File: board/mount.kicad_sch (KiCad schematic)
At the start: 4 parts

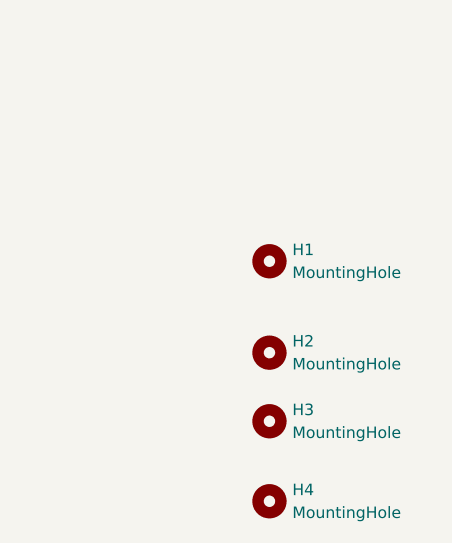
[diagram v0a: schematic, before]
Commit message: Added Servo, cleaned up schematic
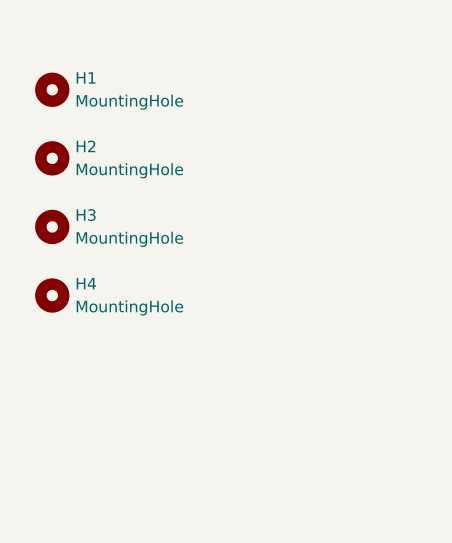
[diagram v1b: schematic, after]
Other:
- moved on the sheet: H1, H2, H3, H4
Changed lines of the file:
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@@
 	(symbol
 		(lib_id "Mechanical:MountingHole")
-		(at 53.34 74.93 0)
+		(at 29.21 52.07 0)
 		(unit 1)
 		(exclude_from_sim no)
@@
 		(fields_autoplaced yes)
 		(property "Reference" "H4"
-			(at 55.88 73.6599 0)
-			(effects
-				(font
-					(size 1.27 1.27)
-				)
-				(justify left)
-			)
-		)
-		(property "Value" "MountingHole"
-			(at 55.88 76.1999 0)
-			(effects
-				(font
-					(size 1.27 1.27)
-				)
-				(justify left)
-			)
-		)
-		(property "Footprint" ""
-			(at 53.34 74.93 0)
-			(effects
-				(font
-					(size 1.27 1.27)
-				)
-				(hide yes)
-			)
-		)
-		(property "Datasheet" "~"
-			(at 53.34 74.93 0)
-			(effects
-				(font
-					(size 1.27 1.27)
-				)
-				(hide yes)
-			)
-		)
-		(property "Description" "Mounting Hole without connection"
-			(at 53.34 74.93 0)
+			(at 31.75 50.7999 0)
+			(effects
+				(font
+					(size 1.27 1.27)
+				)
+				(justify left)
+			)
+		)
+		(property "Value" "MountingHole"
+			(at 31.75 53.3399 0)
+			(effects
+				(font
+					(size 1.27 1.27)
+				)
+				(justify left)
+			)
+		)
+		(property "Footprint" ""
+			(at 29.21 52.07 0)
+			(effects
+				(font
+					(size 1.27 1.27)
+				)
+				(hide yes)
+			)
+		)
+		(property "Datasheet" "~"
+			(at 29.21 52.07 0)
+			(effects
+				(font
+					(size 1.27 1.27)
+				)
+				(hide yes)
+			)
+		)
+		(property "Description" "Mounting Hole without connection"
+			(at 29.21 52.07 0)
 			(effects
 				(font
@@
 	(symbol
 		(lib_id "Mechanical:MountingHole")
-		(at 53.34 58.42 0)
+		(at 29.21 36.83 0)
 		(unit 1)
 		(exclude_from_sim no)
@@
 		(fields_autoplaced yes)
 		(property "Reference" "H2"
-			(at 55.88 57.1499 0)
-			(effects
-				(font
-					(size 1.27 1.27)
-				)
-				(justify left)
-			)
-		)
-		(property "Value" "MountingHole"
-			(at 55.88 59.6899 0)
-			(effects
-				(font
-					(size 1.27 1.27)
-				)
-				(justify left)
-			)
-		)
-		(property "Footprint" ""
-			(at 53.34 58.42 0)
-			(effects
-				(font
-					(size 1.27 1.27)
-				)
-				(hide yes)
-			)
-		)
-		(property "Datasheet" "~"
-			(at 53.34 58.42 0)
-			(effects
-				(font
-					(size 1.27 1.27)
-				)
-				(hide yes)
-			)
-		)
-		(property "Description" "Mounting Hole without connection"
-			(at 53.34 58.42 0)
+			(at 31.75 35.5599 0)
+			(effects
+				(font
+					(size 1.27 1.27)
+				)
+				(justify left)
+			)
+		)
+		(property "Value" "MountingHole"
+			(at 31.75 38.0999 0)
+			(effects
+				(font
+					(size 1.27 1.27)
+				)
+				(justify left)
+			)
+		)
+		(property "Footprint" ""
+			(at 29.21 36.83 0)
+			(effects
+				(font
+					(size 1.27 1.27)
+				)
+				(hide yes)
+			)
+		)
+		(property "Datasheet" "~"
+			(at 29.21 36.83 0)
+			(effects
+				(font
+					(size 1.27 1.27)
+				)
+				(hide yes)
+			)
+		)
+		(property "Description" "Mounting Hole without connection"
+			(at 29.21 36.83 0)
 			(effects
 				(font
@@
 	(symbol
 		(lib_id "Mechanical:MountingHole")
-		(at 53.34 48.26 0)
+		(at 29.21 29.21 0)
 		(unit 1)
 		(exclude_from_sim no)
@@
 		(fields_autoplaced yes)
 		(property "Reference" "H1"
-			(at 55.88 46.9899 0)
-			(effects
-				(font
-					(size 1.27 1.27)
-				)
-				(justify left)
-			)
-		)
-		(property "Value" "MountingHole"
-			(at 55.88 49.5299 0)
-			(effects
-				(font
-					(size 1.27 1.27)
-				)
-				(justify left)
-			)
-		)
-		(property "Footprint" ""
-			(at 53.34 48.26 0)
-			(effects
-				(font
-					(size 1.27 1.27)
-				)
-				(hide yes)
-			)
-		)
-		(property "Datasheet" "~"
-			(at 53.34 48.26 0)
-			(effects
-				(font
-					(size 1.27 1.27)
-				)
-				(hide yes)
-			)
-		)
-		(property "Description" "Mounting Hole without connection"
-			(at 53.34 48.26 0)
+			(at 31.75 27.9399 0)
+			(effects
+				(font
+					(size 1.27 1.27)
+				)
+				(justify left)
+			)
+		)
+		(property "Value" "MountingHole"
+			(at 31.75 30.4799 0)
+			(effects
+				(font
+					(size 1.27 1.27)
+				)
+				(justify left)
+			)
+		)
+		(property "Footprint" ""
+			(at 29.21 29.21 0)
+			(effects
+				(font
+					(size 1.27 1.27)
+				)
+				(hide yes)
+			)
+		)
+		(property "Datasheet" "~"
+			(at 29.21 29.21 0)
+			(effects
+				(font
+					(size 1.27 1.27)
+				)
+				(hide yes)
+			)
+		)
+		(property "Description" "Mounting Hole without connection"
+			(at 29.21 29.21 0)
 			(effects
 				(font
@@
 	(symbol
 		(lib_id "Mechanical:MountingHole")
-		(at 53.34 66.04 0)
+		(at 29.21 44.45 0)
 		(unit 1)
 		(exclude_from_sim no)
@@
 		(fields_autoplaced yes)
 		(property "Reference" "H3"
-			(at 55.88 64.7699 0)
-			(effects
-				(font
-					(size 1.27 1.27)
-				)
-				(justify left)
-			)
-		)
-		(property "Value" "MountingHole"
-			(at 55.88 67.3099 0)
-			(effects
-				(font
-					(size 1.27 1.27)
-				)
-				(justify left)
-			)
-		)
-		(property "Footprint" ""
-			(at 53.34 66.04 0)
-			(effects
-				(font
-					(size 1.27 1.27)
-				)
-				(hide yes)
-			)
-		)
-		(property "Datasheet" "~"
-			(at 53.34 66.04 0)
-			(effects
-				(font
-					(size 1.27 1.27)
-				)
-				(hide yes)
-			)
-		)
-		(property "Description" "Mounting Hole without connection"
-			(at 53.34 66.04 0)
-			(effects
-				(font
+			(at 31.75 43.1799 0)
+			(effects
+				(font
+					(size 1.27 1.27)
+				)
+				(justify left)
+			)
+		)
+		(property "Value" "MountingHole"
+			(at 31.75 45.7199 0)
+			(effects
+				(font
+					(size 1.27 1.27)
+				)
+				(justify left)
+			)
+		)
+		(property "Footprint" ""
+			(at 29.21 44.45 0)
+			(effects
+				(font
+					(size 1.27 1.27)
+				)
+				(hide yes)
+			)
+		)
+		(property "Datasheet" "~"
+			(at 29.21 44.45 0)
+			(effects
+				(font
+					(size 1.27 1.27)
+				)
+				(hide yes)
+			)
+		)
+		(property "Description" "Mounting Hole without connection"
+			(at 29.21 44.45 0)
+			(effects
+				(font

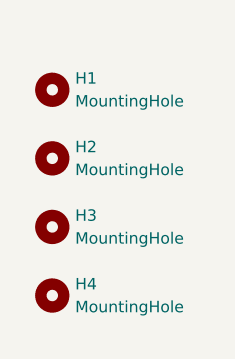
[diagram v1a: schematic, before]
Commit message: Added Labels, Missing Requirements, and Refined Look
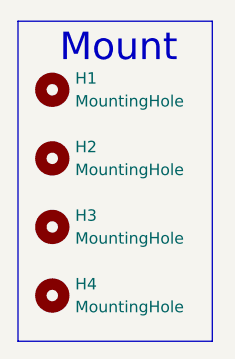
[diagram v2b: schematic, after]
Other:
- note added: "Mount"
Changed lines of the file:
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@@
 	(generator_version "9.0")
 	(paper "A4")
+	(rectangle
+		(start 25.4 21.59)
+		(end 46.99 57.15)
+		(stroke
+			(width 0)
+			(type default)
+		)
+		(fill
+			(type none)
+		)
+	)
+	(text "Mount"
+		(exclude_from_sim no)
+		(at 36.576 24.638 0)
+		(effects
+			(font
+				(face "Calibri")
+				(size 3.048 3.048)
+			)
+		)
+	)
 	(symbol
 		(lib_id "Mechanical:MountingHole")

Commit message: assigned footprints
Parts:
- H1, H2, H3, H4: footprint (none) -> MRDT_Drill_Holes:4_40_Hole_Corner
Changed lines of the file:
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@@
 			)
 		)
-		(property "Footprint" ""
+		(property "Footprint" "MRDT_Drill_Holes:4_40_Hole_Corner"
 			(at 29.21 52.07 0)
 			(effects
@@
 			)
 		)
-		(property "Footprint" ""
+		(property "Footprint" "MRDT_Drill_Holes:4_40_Hole_Corner"
 			(at 29.21 36.83 0)
 			(effects
@@
 			)
 		)
-		(property "Footprint" ""
+		(property "Footprint" "MRDT_Drill_Holes:4_40_Hole_Corner"
 			(at 29.21 29.21 0)
 			(effects
@@
 			)
 		)
-		(property "Footprint" ""
+		(property "Footprint" "MRDT_Drill_Holes:4_40_Hole_Corner"
 			(at 29.21 44.45 0)
 			(effects

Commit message: Final hardware as ordered
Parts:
- H1, H2, H3, H4: footprint MRDT_Drill_Holes:4_40_Hole_Corner -> MRDT_Drill_Holes:4_40_Hole_Pad_Via; symbol Mechanical:MountingHole -> MRDT_Connectors:4_40_Mounting_Hole_Pad; now in the parts list
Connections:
- new net GND: H1.1, H2.1, H3.1, H4.1
